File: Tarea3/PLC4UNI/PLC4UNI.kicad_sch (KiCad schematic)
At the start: 0 parts

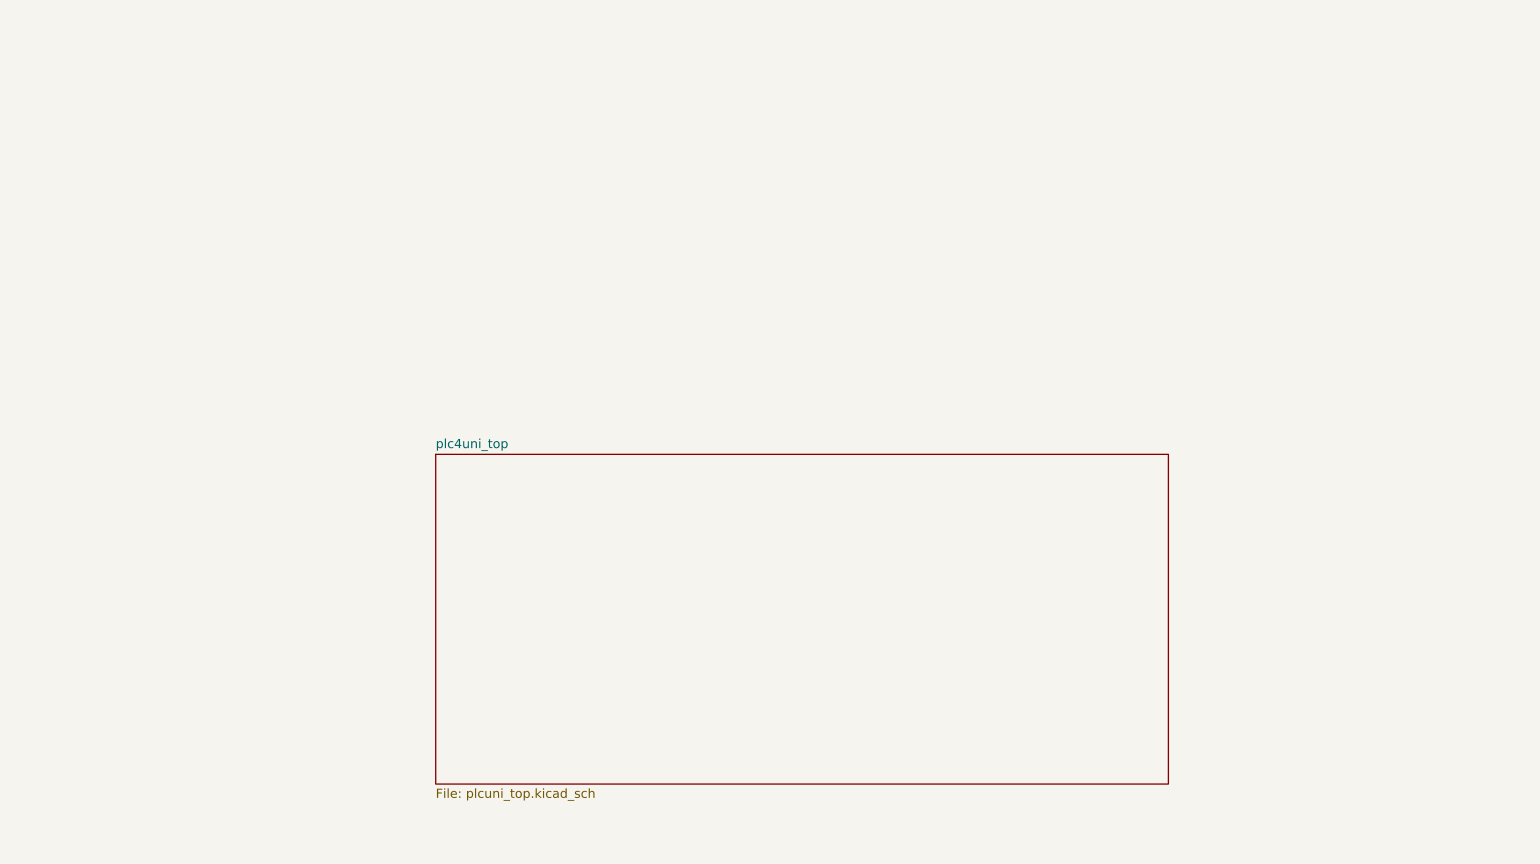
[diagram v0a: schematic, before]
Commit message: Cambio de directorio [Tarea2->CAD]
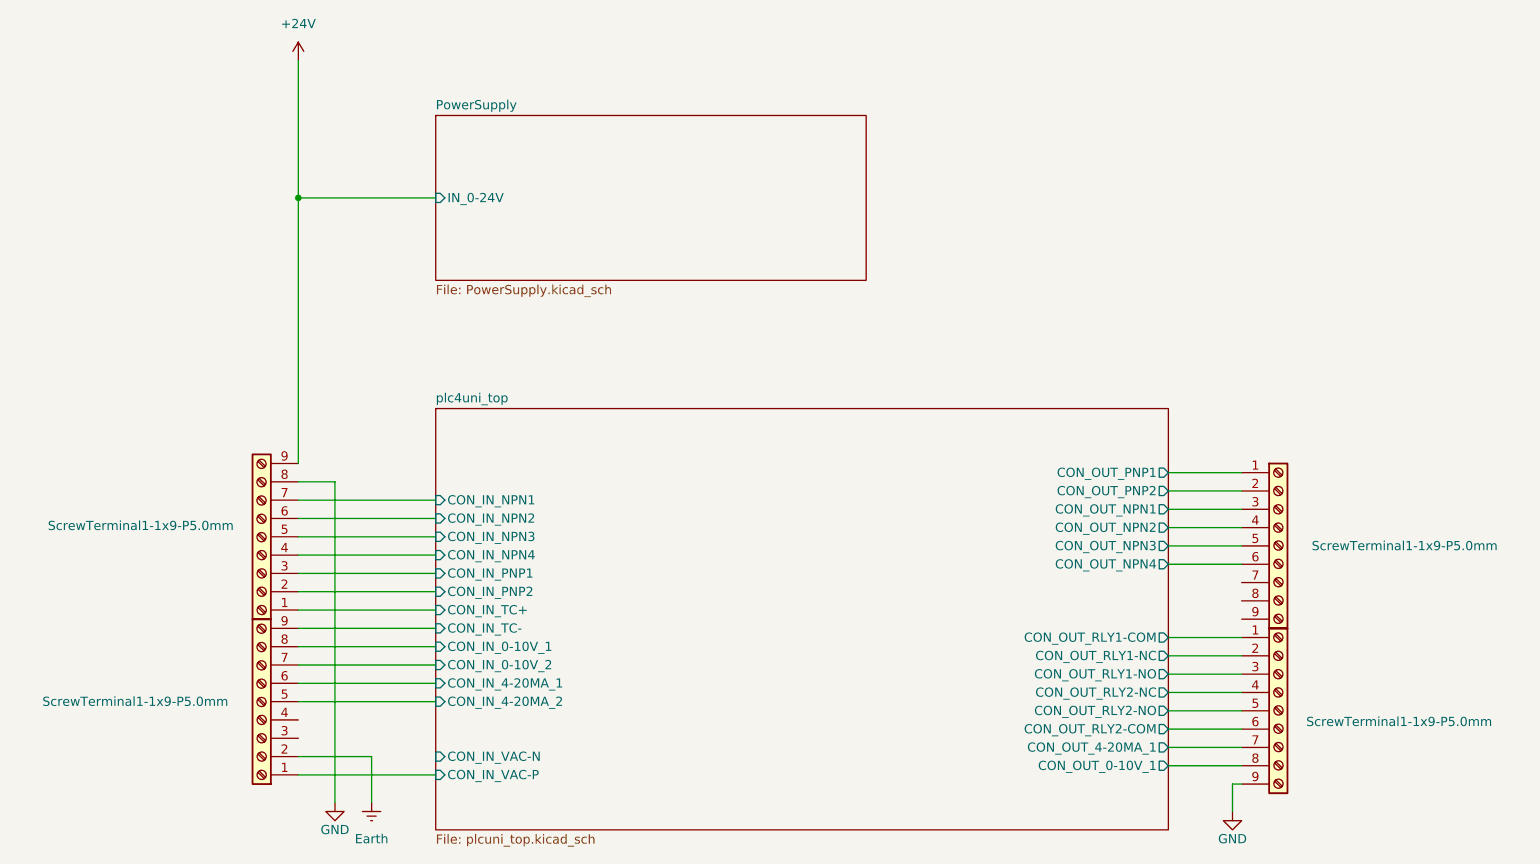
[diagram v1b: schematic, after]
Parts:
- added U1, U2, U3, U4: ScrewTerminal1-1x9-P5.0mm, EasyEDA:CONN-TH_9P-P5.00_DB127V-5.0-9P-GN-S, symbol EasyEDA:ScrewTerminal1-1x9-P5.0mm
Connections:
- new net +24V: U1.9
- new net Earth: U2.2
- new net GND: U1.8, U3.9
- new net plc4uni_top/CON_IN_0-10V_1: U2.8
- new net plc4uni_top/CON_IN_0-10V_2: U2.7
- new net plc4uni_top/CON_IN_4-20MA_1: U2.6
- new net plc4uni_top/CON_IN_4-20MA_2: U2.5
- new net plc4uni_top/CON_IN_NPN1: U1.7
- new net plc4uni_top/CON_IN_NPN2: U1.6
- new net plc4uni_top/CON_IN_NPN3: U1.5
- new net plc4uni_top/CON_IN_NPN4: U1.4
- new net plc4uni_top/CON_IN_PNP1: U1.3
- new net plc4uni_top/CON_IN_PNP2: U1.2
- new net plc4uni_top/CON_IN_TC+: U1.1
- new net plc4uni_top/CON_IN_TC-: U2.9
- new net plc4uni_top/CON_IN_VAC-P: U2.1
- new net plc4uni_top/CON_OUT_0-10V_1: U3.8
- new net plc4uni_top/CON_OUT_4-20MA_1: U3.7
- new net plc4uni_top/CON_OUT_NPN1: U4.3
- new net plc4uni_top/CON_OUT_NPN2: U4.4
- new net plc4uni_top/CON_OUT_NPN3: U4.5
- new net plc4uni_top/CON_OUT_NPN4: U4.6
- new net plc4uni_top/CON_OUT_PNP1: U4.1
- new net plc4uni_top/CON_OUT_PNP2: U4.2
- new net plc4uni_top/CON_OUT_RLY1-COM: U3.1
- new net plc4uni_top/CON_OUT_RLY1-NC: U3.2
- new net plc4uni_top/CON_OUT_RLY1-NO: U3.3
- new net plc4uni_top/CON_OUT_RLY2-COM: U3.6
- new net plc4uni_top/CON_OUT_RLY2-NC: U3.4
- new net plc4uni_top/CON_OUT_RLY2-NO: U3.5
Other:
- added sheet PowerSupply (PowerSupply.kicad_sch)
- sheet plc4uni_top ports: added CON_IN_0-10V_1, CON_IN_0-10V_2, CON_IN_4-20MA_1, CON_IN_4-20MA_2, CON_IN_NPN1, CON_IN_NPN2, CON_IN_NPN3, CON_IN_NPN4, CON_IN_PNP1, CON_IN_PNP2, CON_IN_TC+, CON_IN_TC-, CON_IN_VAC-N, CON_IN_VAC-P, CON_OUT_0-10V_1, CON_OUT_4-20MA_1, CON_OUT_NPN1, CON_OUT_NPN2, CON_OUT_NPN3, CON_OUT_NPN4, CON_OUT_PNP1, CON_OUT_PNP2, CON_OUT_RLY1-COM, CON_OUT_RLY1-NC, CON_OUT_RLY1-NO, CON_OUT_RLY2-COM, CON_OUT_RLY2-NC, CON_OUT_RLY2-NO; removed none
